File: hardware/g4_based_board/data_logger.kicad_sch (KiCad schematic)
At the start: 13 parts, among them J1 Conn_01x07_Socket, J2 Conn_02x07_Odd_Even, J3 Conn_01x07_Socket

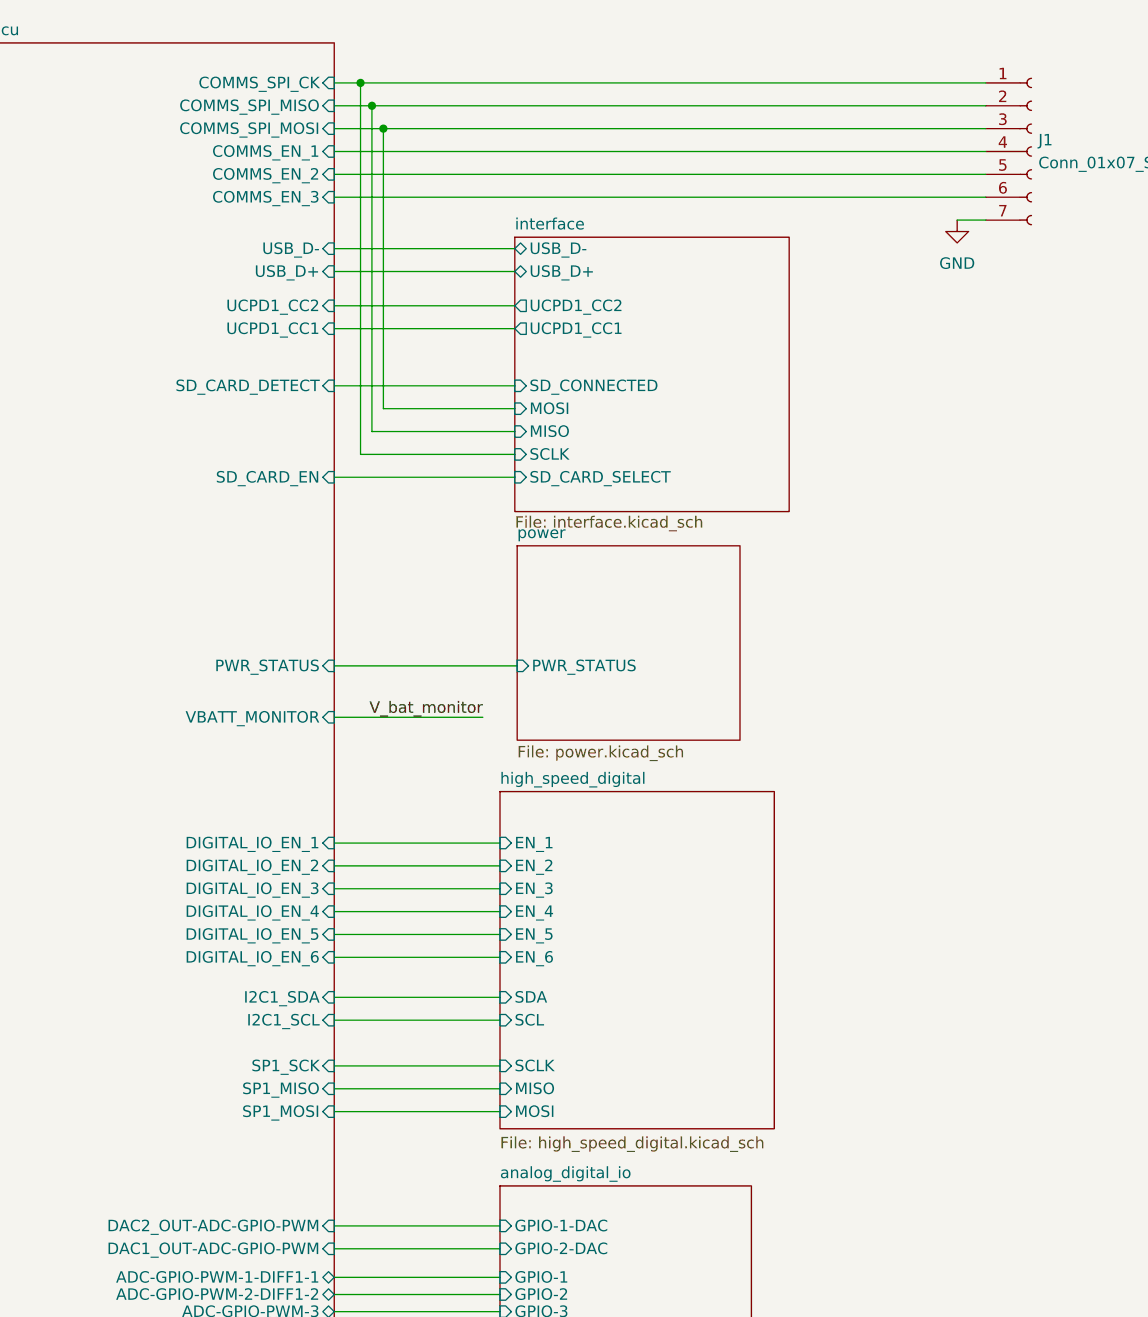
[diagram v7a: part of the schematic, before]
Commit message: added usart header and attached buttons
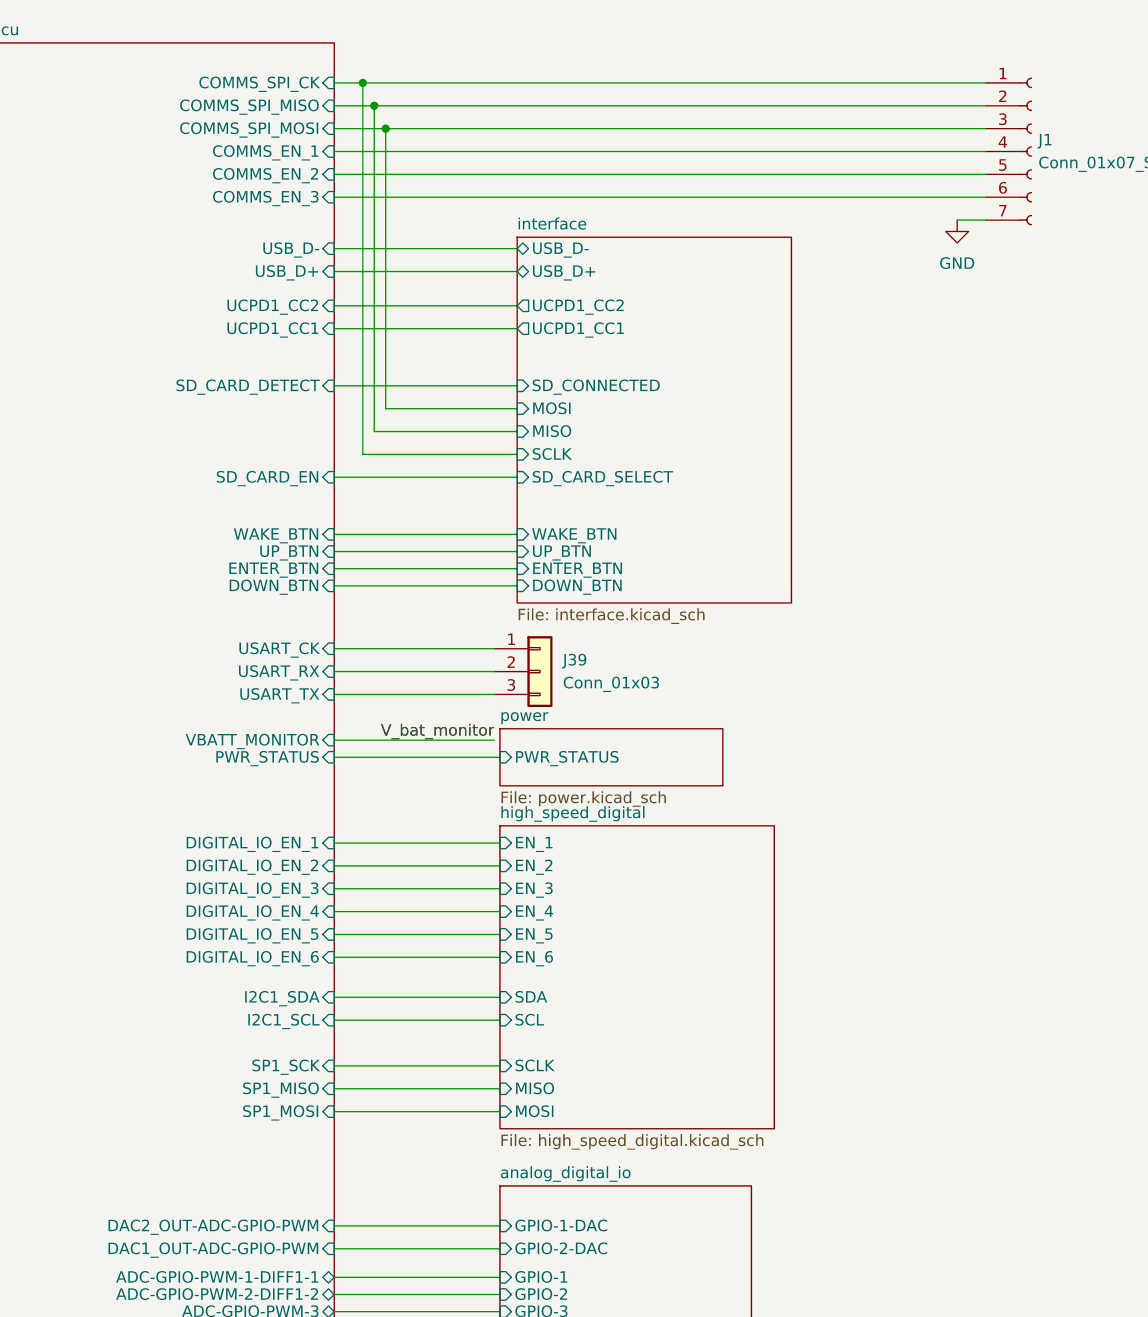
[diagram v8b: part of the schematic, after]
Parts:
- added J39: Conn_01x03, Connector_PinHeader_2.54mm:PinHeader_1x03_P2.54mm_Vertical, symbol Connector_Generic:Conn_01x03
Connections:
- new net mcu/USART_CK: J39.1 (Pin_1)
- new net mcu/USART_RX: J39.2 (Pin_2)
- new net mcu/USART_TX: J39.3 (Pin_3)
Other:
- sheet interface ports: added DOWN_BTN, ENTER_BTN, UP_BTN, WAKE_BTN; removed none
- sheet mcu ports: added DOWN_BTN, ENTER_BTN, UP_BTN, USART_CK, USART_RX, USART_TX, WAKE_BTN; removed none
